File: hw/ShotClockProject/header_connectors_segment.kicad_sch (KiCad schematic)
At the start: 13 parts, among them J10 DW254W-22-20-85, J7 DW254W-22-20-85, J8 DW254W-22-20-85, J9 DW254W-22-20-85, Q1 Q_NPN_BCE, Q1 Q_PMOS_SGD

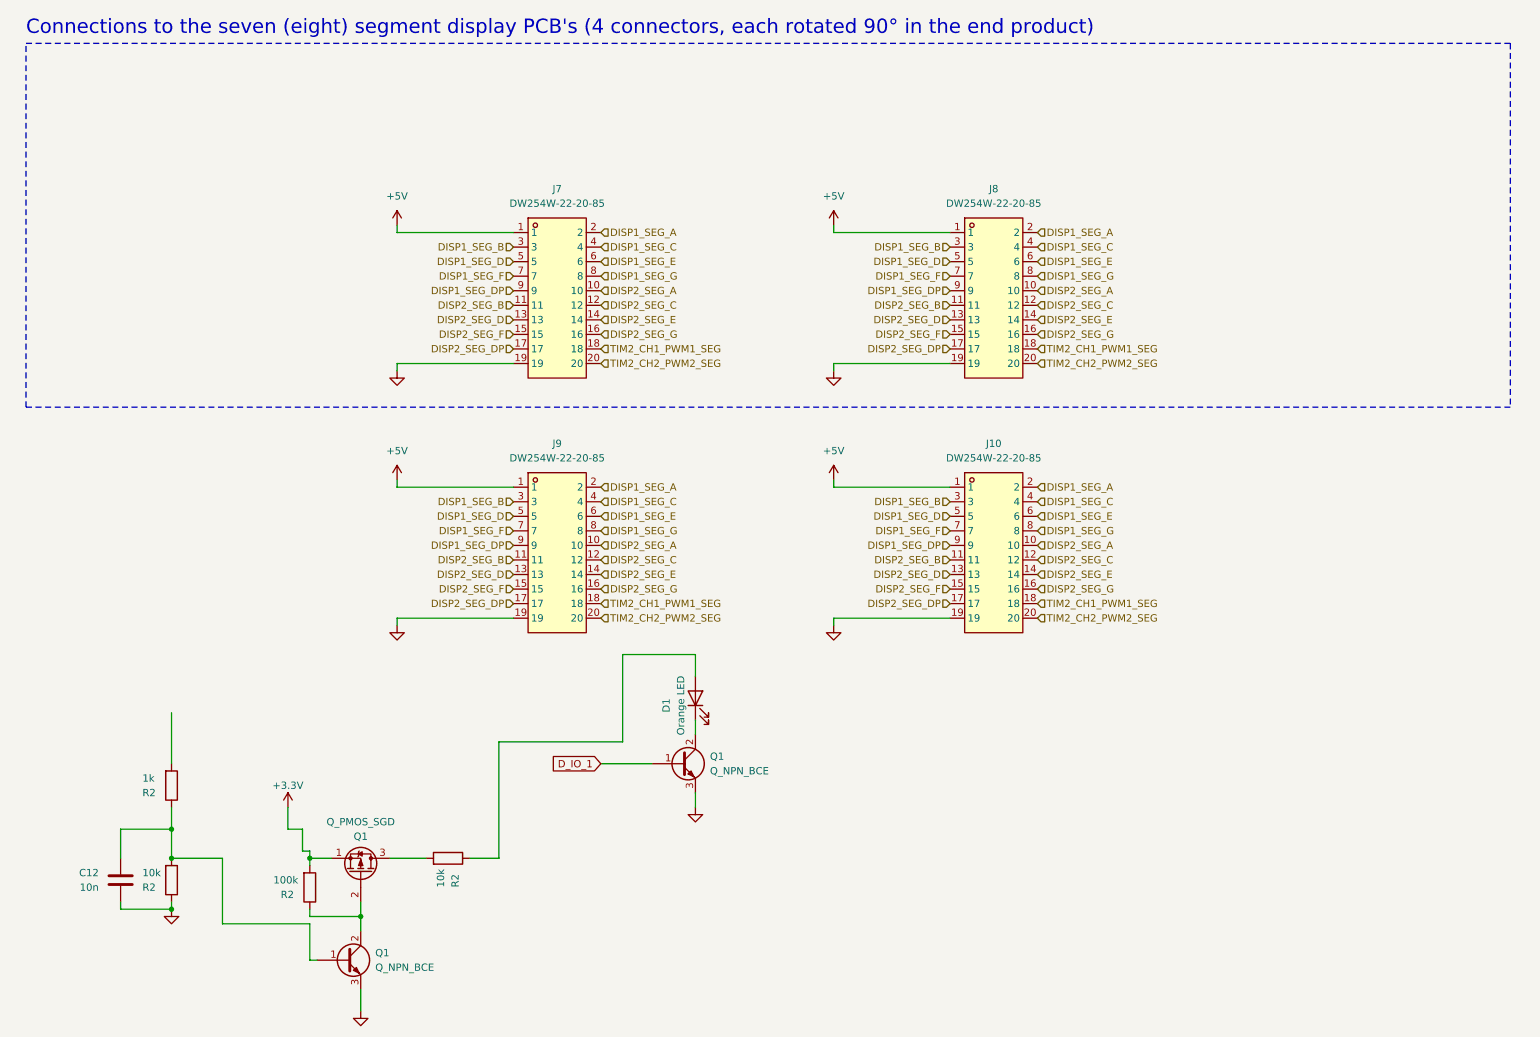
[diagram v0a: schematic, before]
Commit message: Finshed both schematics
- LED driving transistors are placed
- All connectors on segment display PCB are placed
- All schematic references have been re-configured (autosort on Y axis)
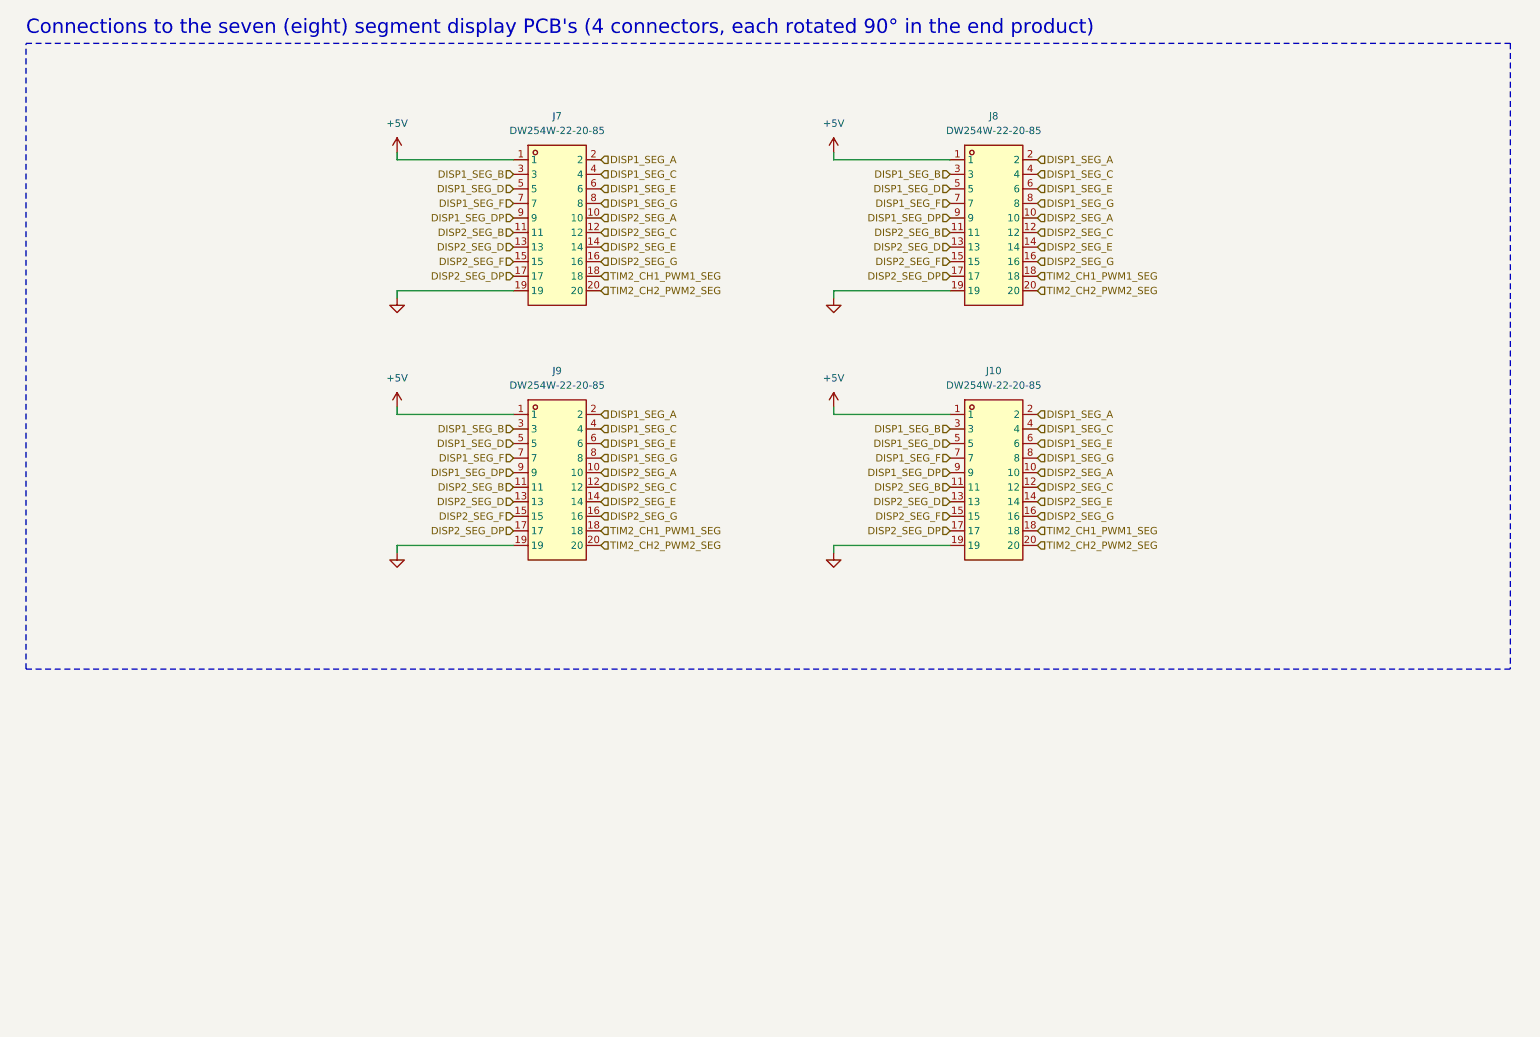
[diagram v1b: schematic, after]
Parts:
- removed C12: 10n, Capacitor_SMD:C_0603_1608Metric, symbol Device:C
- removed D1: Orange LED, LED_SMD:LED_0603_1608Metric, symbol Device:LED
- removed Q1 (x2): Q_NPN_BCE, Package_TO_SOT_SMD:SOT-23, symbol Device:Q_NPN_BCE
- removed Q1: Q_PMOS_SGD, symbol Device:Q_PMOS_SGD
- removed R2: 1k, Resistor_SMD:R_0402_1005Metric, symbol Device:R
- removed R2 (x2): 10k, Resistor_SMD:R_0402_1005Metric, symbol Device:R
- removed R2: 100k, Resistor_SMD:R_0402_1005Metric, symbol Device:R
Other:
- moved on the sheet: J10, J7, J8, J9

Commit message: Add FPC conenctors
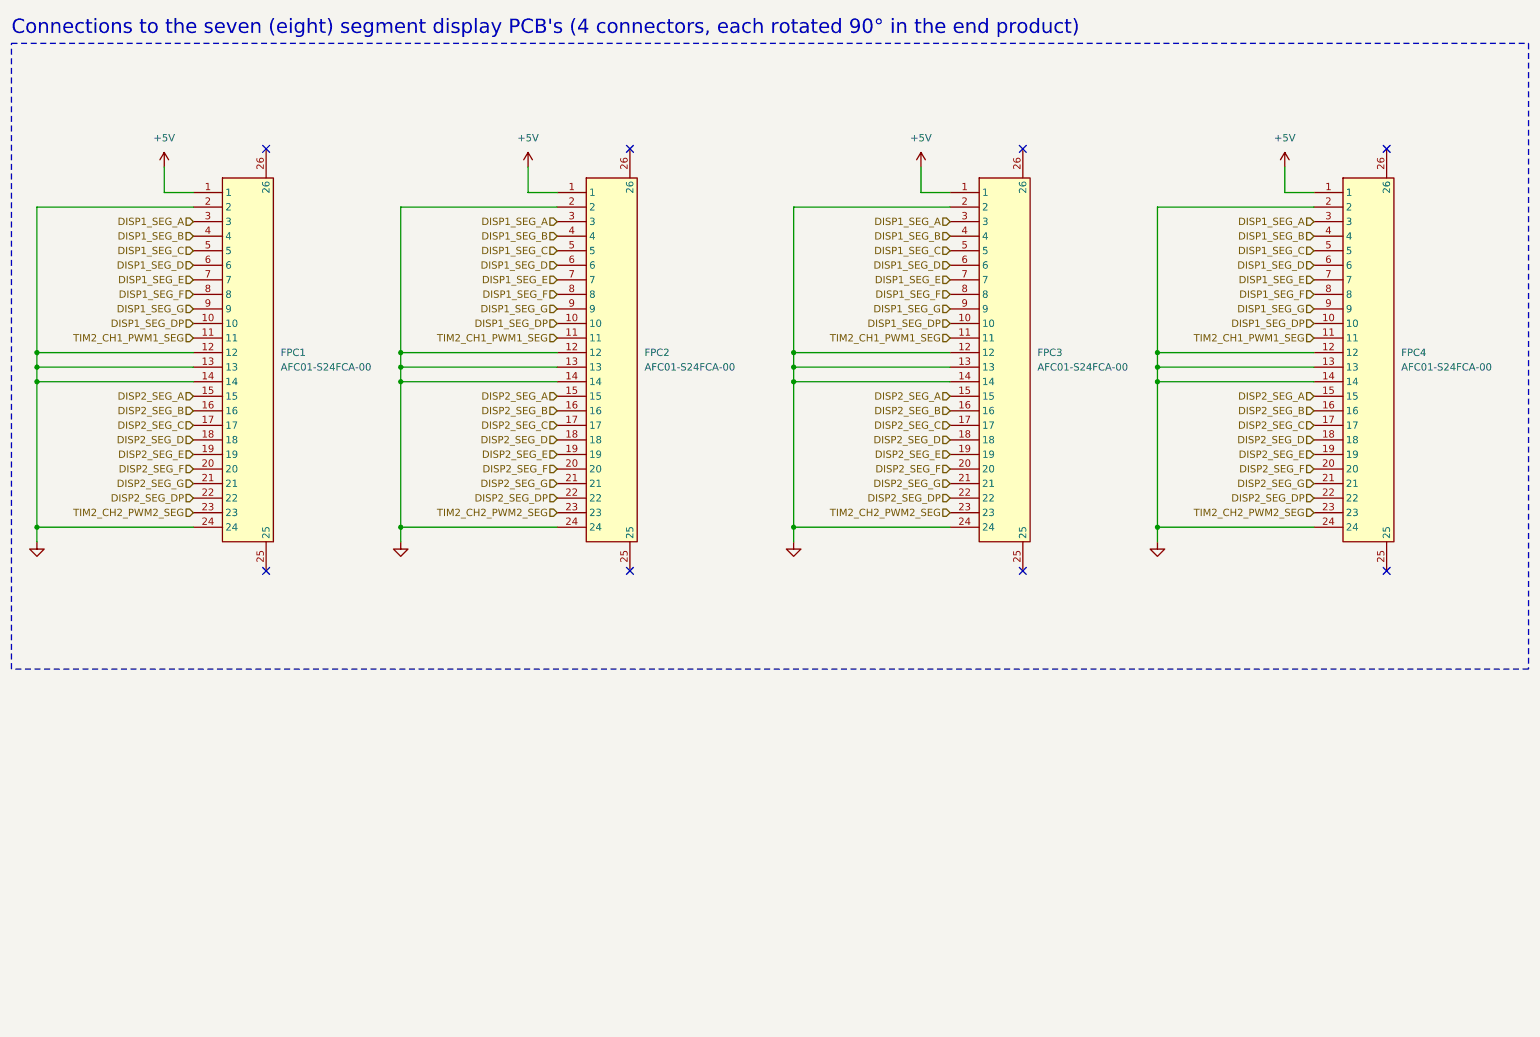
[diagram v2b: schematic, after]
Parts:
- removed J10, J7, J8, J9: DW254W-22-20-85, DW254W-22-20-85:CONN-TH_20P-P2.54_DEALON_DW254W-22-20-85, symbol DW254W-22-20-85:DW254W-22-20-85
- added FPC1, FPC2, FPC3, FPC4: AFC01-S24FCA-00, AFC01-S24FCA-00:FPC-SMD_P0.50-24P_FGS-XJ-H2.0, symbol AFC01-S24FCA-00:AFC01-S24FCA-00
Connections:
- net +5V: now also FPC1.1, FPC2.1, FPC3.1, FPC4.1
- net DISP1_SEG_A: now also FPC1.3, FPC2.3, FPC3.3, FPC4.3
- net DISP1_SEG_B: now also FPC1.4, FPC2.4, FPC3.4, FPC4.4
- net DISP1_SEG_C: now also FPC1.5, FPC2.5, FPC3.5, FPC4.5
- net DISP1_SEG_D: now also FPC1.6, FPC2.6, FPC3.6, FPC4.6
- net DISP1_SEG_DP: now also FPC1.10, FPC2.10, FPC3.10, FPC4.10
- net DISP1_SEG_E: now also FPC1.7, FPC2.7, FPC3.7, FPC4.7
- net DISP1_SEG_F: now also FPC1.8, FPC2.8, FPC3.8, FPC4.8
- net DISP1_SEG_G: now also FPC1.9, FPC2.9, FPC3.9, FPC4.9
- net DISP2_SEG_A: now also FPC1.15, FPC2.15, FPC3.15, FPC4.15
- net DISP2_SEG_B: now also FPC1.16, FPC2.16, FPC3.16, FPC4.16
- net DISP2_SEG_C: now also FPC1.17, FPC2.17, FPC3.17, FPC4.17
- net DISP2_SEG_D: now also FPC1.18, FPC2.18, FPC3.18, FPC4.18
- net DISP2_SEG_DP: now also FPC1.22, FPC2.22, FPC3.22, FPC4.22
- net DISP2_SEG_E: now also FPC1.19, FPC2.19, FPC3.19, FPC4.19
- net DISP2_SEG_F: now also FPC1.20, FPC2.20, FPC3.20, FPC4.20
- net DISP2_SEG_G: now also FPC1.21, FPC2.21, FPC3.21, FPC4.21
- net GND: now also FPC1.12, FPC1.13, FPC1.14, FPC1.2, FPC1.24, FPC2.12, FPC2.13, FPC2.14, FPC2.2, FPC2.24, FPC3.12, FPC3.13, FPC3.14, FPC3.2, FPC3.24, FPC4.12, FPC4.13, FPC4.14, FPC4.2, FPC4.24
- net TIM2_CH1_PWM1_SEG: now also FPC1.11, FPC2.11, FPC3.11, FPC4.11
- net TIM2_CH2_PWM2_SEG: now also FPC1.23, FPC2.23, FPC3.23, FPC4.23
- no-connect marks 0 -> 8

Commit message: Added LCSC Part number
Renamed output folders
Created first output files for REV1
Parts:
- FPC1, FPC2, FPC3, FPC4: LCSC Part # (none) -> C262669
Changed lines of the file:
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@@
       (effects (font (size 1.27 1.27)) hide)
     )
-    (property "LCSC Part" "C262669" (at 186.69 127.635 0)
+    (property "LCSC Part #" "C262669" (at 186.69 78.105 0)
+      (effects (font (size 1.27 1.27)) hide)
+    )
+    (property "LCSC Part" "C262669" (at 186.69 78.105 0)
       (effects (font (size 1.27 1.27)) hide)
     )
@@
       (effects (font (size 1.27 1.27)) hide)
     )
-    (property "LCSC Part" "C262669" (at 54.61 127.635 0)
+    (property "LCSC Part #" "C262669" (at 54.61 78.105 0)
+      (effects (font (size 1.27 1.27)) hide)
+    )
+    (property "LCSC Part" "C262669" (at 54.61 78.105 0)
       (effects (font (size 1.27 1.27)) hide)
     )
@@
       (effects (font (size 1.27 1.27)) hide)
     )
-    (property "LCSC Part" "C262669" (at 118.11 127.635 0)
+    (property "LCSC Part #" "C262669" (at 118.11 78.105 0)
+      (effects (font (size 1.27 1.27)) hide)
+    )
+    (property "LCSC Part" "C262669" (at 118.11 78.105 0)
       (effects (font (size 1.27 1.27)) hide)
     )
@@
       (effects (font (size 1.27 1.27)) hide)
     )
-    (property "LCSC Part" "C262669" (at 250.19 127.635 0)
-      (effects (font (size 1.27 1.27)) hide)
-    )
+    (property "LCSC Part #" "C262669" (at 250.19 78.105 0)
+      (effects (font (size 1.27 1.27)) hide)
+    )
+    (property "LCSC Part" "C262669" (at 250.19 78.105 0)
+      (effects (font (size 1.27 1.27)) hide)
+    )

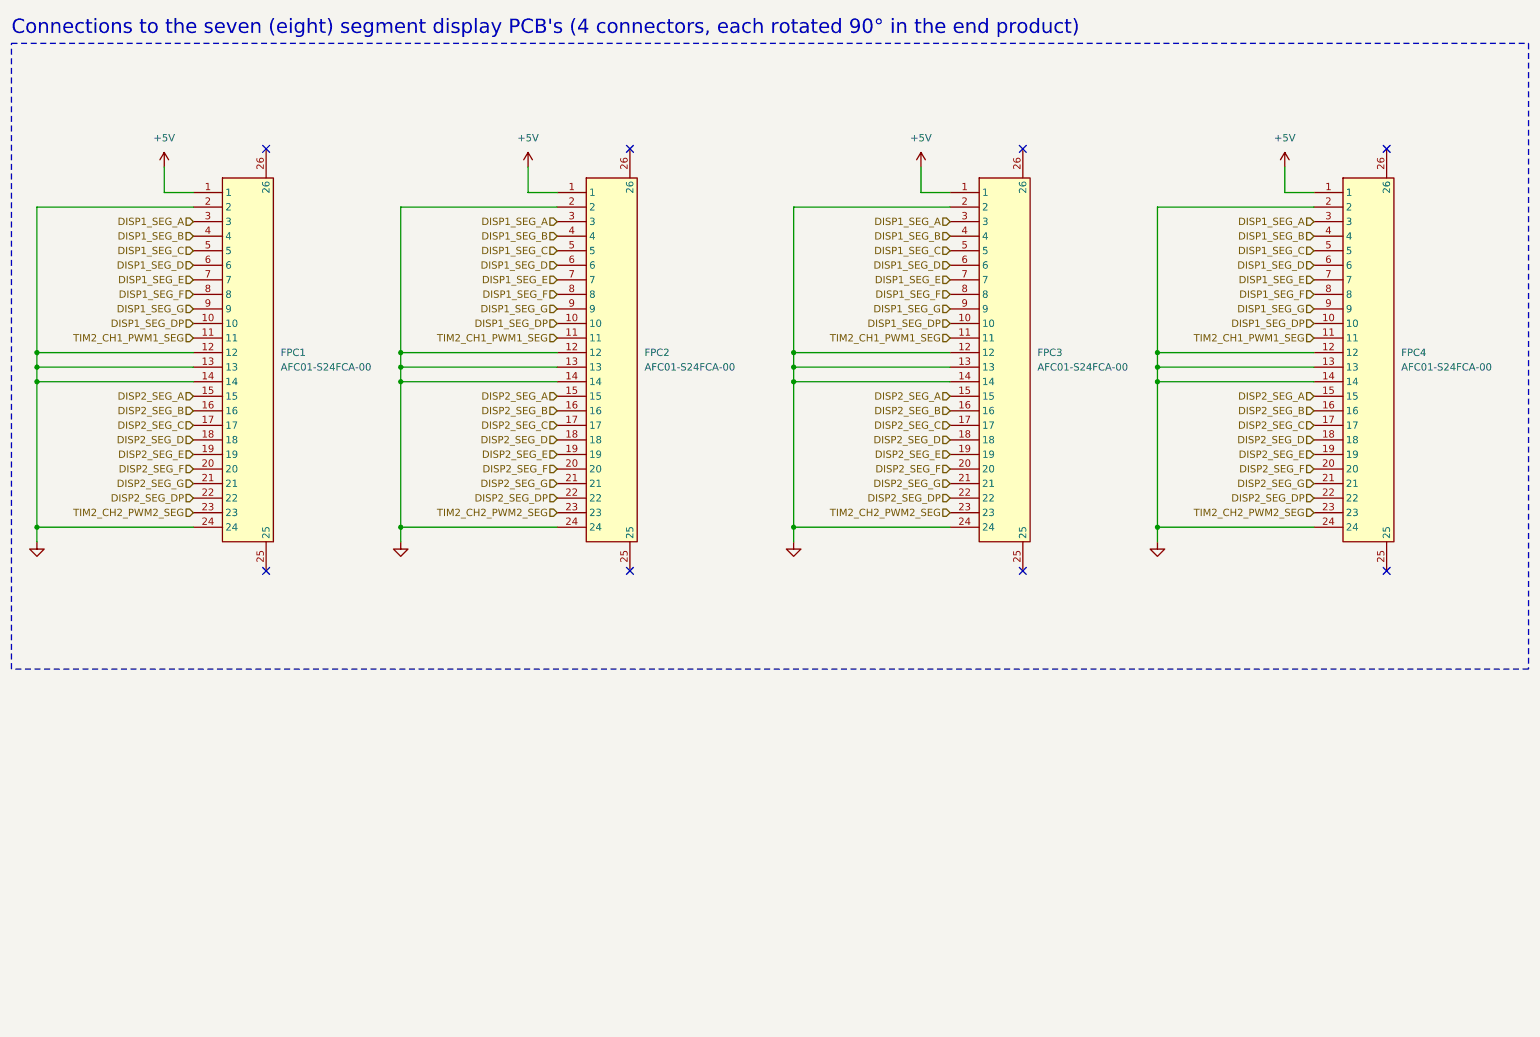
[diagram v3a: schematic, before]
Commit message: Added I2C support
Calculated pull-up resistor values
Added 6 pin female headers to mainboard
Added nRESET line for the I2C chips
Removed PCB routing and part placement
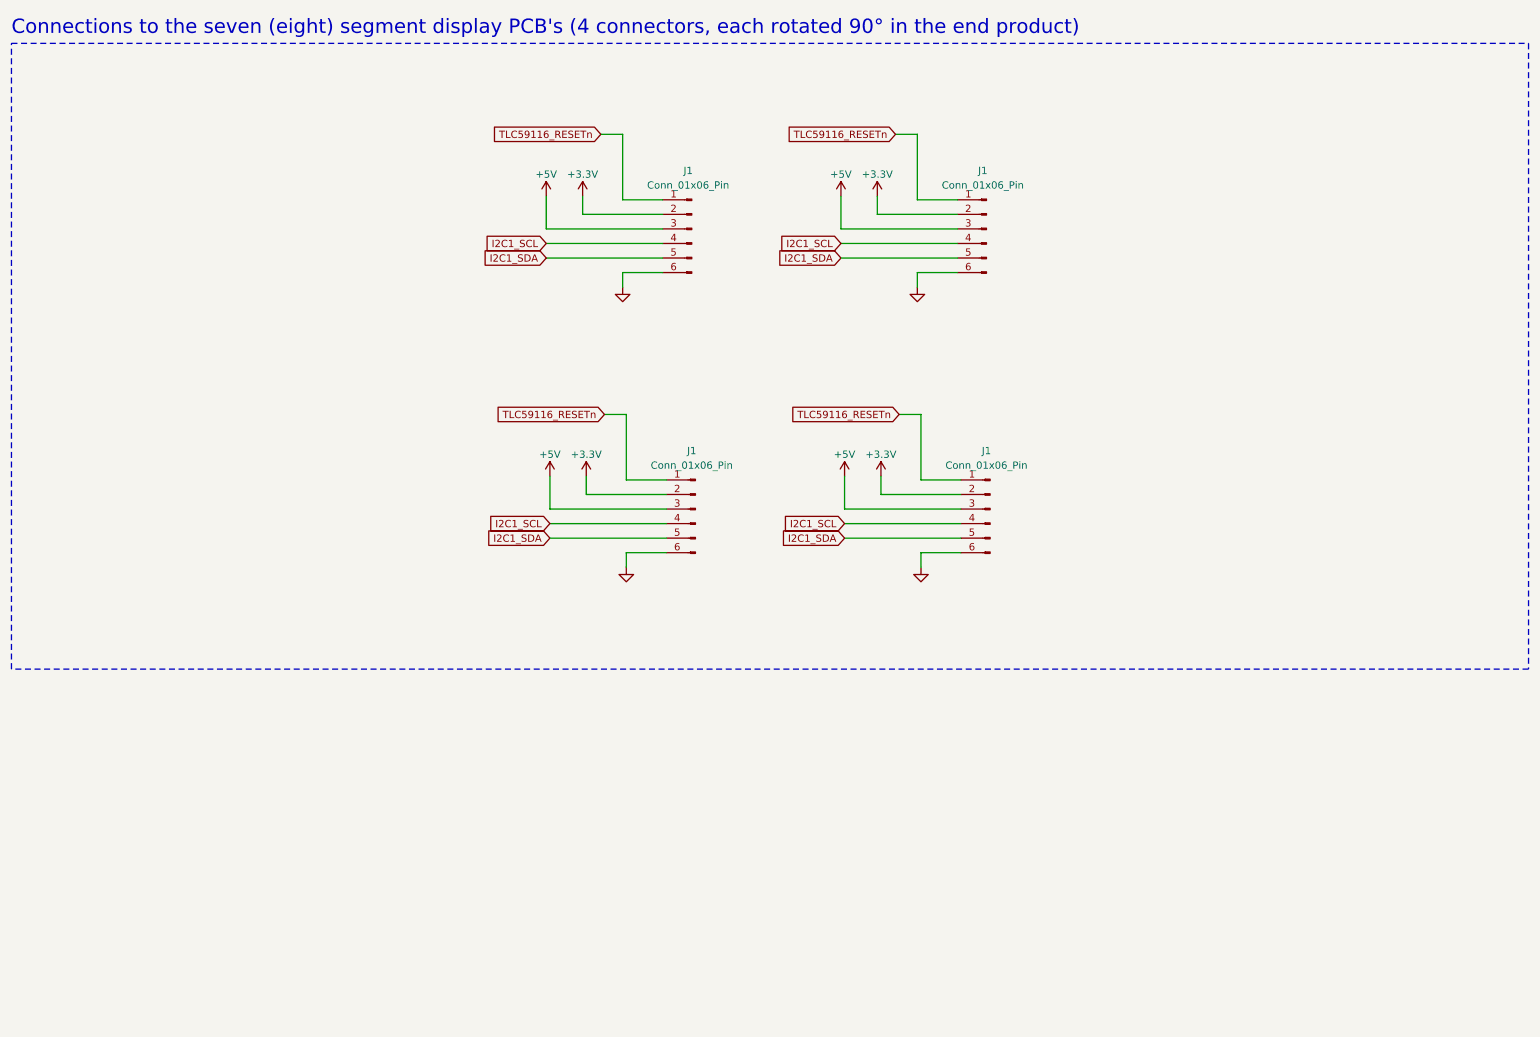
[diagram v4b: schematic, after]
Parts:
- removed FPC1, FPC2, FPC3, FPC4: AFC01-S24FCA-00, AFC01-S24FCA-00:FPC-SMD_P0.50-24P_FGS-XJ-H2.0, symbol AFC01-S24FCA-00:AFC01-S24FCA-00
- added J1 (x4): Conn_01x06_Pin, Connector_PinSocket_2.54mm:PinSocket_1x06_P2.54mm_Horizontal, symbol Connector:Conn_01x06_Pin
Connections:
- net +5V: now also J1.3 (Pin_3), J1.3 (Pin_3), J1.3 (Pin_3), J1.3 (Pin_3)
- net GND: now also J1.6 (Pin_6), J1.6 (Pin_6), J1.6 (Pin_6), J1.6 (Pin_6)
- new net +3.3V: J1.2 (Pin_2), J1.2 (Pin_2), J1.2 (Pin_2), J1.2 (Pin_2)
- new net I2C1_SCL: J1.4 (Pin_4), J1.4 (Pin_4), J1.4 (Pin_4), J1.4 (Pin_4)
- new net I2C1_SDA: J1.5 (Pin_5), J1.5 (Pin_5), J1.5 (Pin_5), J1.5 (Pin_5)
- new net TLC59116_RESETn: J1.1 (Pin_1), J1.1 (Pin_1), J1.1 (Pin_1), J1.1 (Pin_1)
- no-connect marks 8 -> 0
